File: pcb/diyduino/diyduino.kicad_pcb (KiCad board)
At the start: 2 copper layers, 42 parts, among them J1 Conn_Coaxial_Power, U1 ATMEGA328-PU, U2 L7805, Y1 16MHz

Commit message: Reworked the ditduino.
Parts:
- removed A0, A1, A2, A3, A4, A5, D10, DA2, DA3, DA4, DA5, DA6, DA7, DA8, DA9, MISO1, MOSI1, RXD1, SCK1, SCL1, SDA1, TXD1: DATA, Pin_Headers:Pin_Header_Straight_1x03_Pitch2.54mm
- removed J1: Conn_Coaxial_Power, Connectors:BARREL_JACK
- LED3: footprint LEDs:LED_D3.0mm -> LEDs:LED_Rectangular_W3.0mm_H2.0mm
- moved RESET1 37.7 mm to (148.6, 72.4), turned to 180 degrees
- moved PR2 34.7 mm to (118.1, 53.3), turned to 180 degrees
- moved LED3 29.1 mm to (120.0, 59.1)
- moved C4 26.4 mm to (123.8, 72.4), turned to 90 degrees
- moved U2 25.4 mm to (118.7, 66.0)
- moved C5 20.1 mm to (123.8, 62.9), turned to 270 degrees
- moved R1 19.1 mm to (139.7, 65.4), turned to 0 degrees
- moved FT1 12.6 mm to (113.7, 69.8), turned to 180 degrees
- moved U1 8.98 mm to (111.8, 49.5)
- moved Y1 8.47 mm to (137.2, 55.9)
- moved C3 4.96 mm to (139.7, 57.8), turned to 90 degrees
- moved C2 4.26 mm to (134.6, 59.1), turned to 0 degrees
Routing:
- net /RESET: track 19.6 -> 74.9 mm, vias 0 -> 3
- net /VCC: track 158.9 -> 198.9 mm, vias 0 -> 1
- net /VIN: track 107.4 -> 125.0 mm
- net Earth: track 15.4 -> 0.00 mm
- net /D13: track 19.2 -> 7.62 mm
- net /D12: track 18.6 -> 7.62 mm
- net /D11: track 18.1 -> 7.62 mm
- net /D10: track 18.1 -> 7.62 mm
- net /D1: track 56.0 -> 65.1 mm
- net /D5: track 20.6 -> 26.5 mm
- net /A2: track 35.8 -> 40.8 mm, vias 0 -> 1
- net /A3: track 36.9 -> 41.9 mm, vias 0 -> 1
- net Net-(C2-Pad1): track 5.94 -> 10.7 mm
- net /D3: track 35.9 -> 40.1 mm
- net /D4: track 34.6 -> 38.8 mm
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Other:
- board text added: "A0"
- board text added: "A1"
- board text added: "A2"
- board text added: "A3"
- board text added: "A4"
- board text added: "A5"
- board text added: "MISO"
- board text added: "SCK"
- board text removed: "10"
- board text removed: "11"
- board text removed: "12"
- board text removed: "13"

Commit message: Reworked diyduino module.
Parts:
- added D1: D, Diodes_THT:D_T-1_P5.08mm_Horizontal, F.Cu at (116.8, 73.0)
- added D2: D, Diodes_THT:D_T-1_P5.08mm_Horizontal, F.Cu at (122.6, 59.1)
- moved PR2 29.5 mm to (146.1, 62.9)
- moved LED3 24.4 mm to (144.1, 55.2), turned to 270 degrees
- moved R1 6.35 mm to (146.1, 65.4), turned to 180 degrees
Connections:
- FT1 pad 3: /VCC -> Net-(D1-Pad2)
- U2 pad 3: /VCC -> Net-(D2-Pad2)
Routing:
- net /VCC: track 198.9 -> 161.0 mm
- net Net-(D1-Pad2): track 0.00 -> 16.2 mm
- net Net-(D2-Pad2): track 0.00 -> 4.97 mm
- net Net-(LED3-Pad2): track 3.96 -> 5.87 mm
- net /D9: track 33.9 -> 32.9 mm
- net /D7: track 22.4 -> 23.3 mm
- net /D0: track 57.4 -> 56.9 mm

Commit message: Tidied diyduino
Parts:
- moved D1 1.91 mm to (118.7, 73.0), turned to 180 degrees
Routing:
- net Net-(D1-Pad2): track 16.2 -> 11.1 mm
- net /RESET: track 74.8 -> 72.5 mm, vias 3 -> 1
- net /D0: track 56.9 -> 58.3 mm
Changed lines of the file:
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@@
     (thickness 1.6)
     (drawings 36)
-    (tracks 222)
+    (tracks 226)
     (zones 0)
     (modules 21)
@@
   )
   (setup
-    (last_trace_width 0.25)
+    (last_trace_width 0.5)
     (user_trace_width 0.5)
     (user_trace_width 0.5)
@@
     (pad_to_mask_clearance 0)
     (aux_axis_origin 0 0)
-    (visible_elements FFFFFF7F)
+    (visible_elements FFFEFF7F)
     (pcbplotparams
       (layerselection 0x00030_80000001)
@@
     (descr "CP, Radial series, Radial, pin pitch=2.50mm, , diameter=6.3mm, Electrolytic Capacitor")
     (tags "CP Radial series Radial pin pitch 2.50mm  diameter 6.3mm Electrolytic Capacitor")
-    (fp_text reference C4 (at 1.25 -4.46 90) (layer F.SilkS)
+    (fp_text reference C4 (at -1.27 -2.54 180) (layer F.SilkS)
       (effects (font (size 1 1) (thickness 0.15)))
     )
@@
     (descr "CP, Radial series, Radial, pin pitch=2.50mm, , diameter=6.3mm, Electrolytic Capacitor")
     (tags "CP Radial series Radial pin pitch 2.50mm  diameter 6.3mm Electrolytic Capacitor")
-    (fp_text reference C5 (at 1.25 -4.46 270) (layer F.SilkS)
+    (fp_text reference C5 (at -1.27 -2.54 360) (layer F.SilkS)
       (effects (font (size 1 1) (thickness 0.15)))
     )
@@
     (descr https://www.omron.com/ecb/products/pdf/en-b3f.pdf)
     (tags "tact sw push 6mm")
-    (fp_text reference RESET1 (at 3.175 3.81 180) (layer F.SilkS)
+    (fp_text reference RESET1 (at 3.175 2.54 180) (layer F.SilkS)
       (effects (font (size 1 1) (thickness 0.15)))
     )
@@
       (effects (font (size 1 1) (thickness 0.15)))
     )
-    (fp_text user %R (at 3.25 2.25 180) (layer F.Fab)
+    (fp_text user %R (at 3.175 2.54 180) (layer F.Fab)
       (effects (font (size 1 1) (thickness 0.15)))
     )
@@
   )
   (module Diodes_THT:D_T-1_P5.08mm_Horizontal (layer F.Cu)
-    (at 116.84 73.025 270)
+    (at 118.745 73.025 180)
     (descr "D, T-1 series, Axial, Horizontal, pin pitch=5.08mm, , length*diameter=3.2*2.6mm^2, , http://www.diodes.com/_files/packages/T-1.pdf")
     (tags "D T-1 series Axial Horizontal pin pitch 5.08mm  length 3.2mm diameter 2.6mm")
-    (fp_text reference D1 (at 2.54 0 270) (layer F.SilkS)
-      (effects (font (size 1 1) (thickness 0.15)))
-    )
-    (fp_text value D (at 2.54 2.36 270) (layer F.Fab)
-      (effects (font (size 1 1) (thickness 0.15)))
-    )
-    (fp_text user %R (at 2.54 0 270) (layer F.Fab)
+    (fp_text reference D1 (at 2.54 0 180) (layer F.SilkS)
+      (effects (font (size 1 1) (thickness 0.15)))
+    )
+    (fp_text value D (at 2.54 2.36 180) (layer F.Fab)
+      (effects (font (size 1 1) (thickness 0.15)))
+    )
+    (fp_text user %R (at 2.54 0 180) (layer F.Fab)
       (effects (font (size 1 1) (thickness 0.15)))
     )
@@
     (fp_line (start 6.35 1.65) (end 6.35 -1.65) (layer F.CrtYd) (width 0.05))
     (fp_line (start 6.35 -1.65) (end -1.25 -1.65) (layer F.CrtYd) (width 0.05))
-    (pad 1 thru_hole rect (at 0 0 270) (size 2 2) (drill 1) (layers *.Cu *.Mask)
+    (pad 1 thru_hole rect (at 0 0 180) (size 2 2) (drill 1) (layers *.Cu *.Mask)
       (net 21 /VCC))
-    (pad 2 thru_hole oval (at 5.08 0 270) (size 2 2) (drill 1) (layers *.Cu *.Mask)
+    (pad 2 thru_hole oval (at 5.08 0 180) (size 2 2) (drill 1) (layers *.Cu *.Mask)
       (net 28 "Net-(D1-Pad2)"))
     (model ${KISYS3DMOD}/Diodes_THT.3dshapes/D_T-1_P5.08mm_Horizontal.wrl
@@
   (segment (start 114.935 47.625) (end 111.76 47.625) (width 0.25) (layer F.Cu) (net 14))
   (segment (start 144.78 34.29) (end 144.78 34.925) (width 0.25) (layer B.Cu) (net 14) (status 30))
-  (segment (start 113.665 59.69) (end 114.935 58.42) (width 0.25) (layer B.Cu) (net 15) (status 10))
-  (segment (start 114.935 50.165) (end 114.3 49.53) (width 0.25) (layer B.Cu) (net 15) (status 20))
-  (segment (start 114.935 58.42) (end 114.935 50.165) (width 0.25) (layer B.Cu) (net 15))
+  (segment (start 113.665 59.69) (end 113.03 59.69) (width 0.25) (layer B.Cu) (net 15))
+  (segment (start 113.03 59.69) (end 111.76 58.42) (width 0.25) (layer B.Cu) (net 15))
+  (segment (start 111.76 58.42) (end 111.76 55.245) (width 0.25) (layer B.Cu) (net 15))
+  (segment (start 111.76 55.245) (end 114.3 52.705) (width 0.25) (layer B.Cu) (net 15))
+  (segment (start 114.3 52.705) (end 114.3 49.53) (width 0.25) (layer B.Cu) (net 15))
   (via (at 133.35 39.37) (size 0.6) (drill 0.4) (layers F.Cu B.Cu) (net 15))
   (via (at 118.11 39.37) (size 0.6) (drill 0.4) (layers F.Cu B.Cu) (net 15))
@@
   (segment (start 154.94 53.975) (end 145.415 44.45) (width 0.25) (layer F.Cu) (net 20) (status 10))
   (segment (start 145.415 44.45) (end 126.365 44.45) (width 0.25) (layer F.Cu) (net 20))
-  (segment (start 138.43 62.865) (end 123.825 62.865) (width 0.5) (layer B.Cu) (net 21) (status 30))
+  (segment (start 138.43 65.405) (end 137.795 65.405) (width 0.5) (layer B.Cu) (net 21) (status C00000))
+  (segment (start 137.795 65.405) (end 135.255 62.865) (width 0.5) (layer B.Cu) (net 21) (status 400000))
+  (segment (start 135.255 62.865) (end 123.825 62.865) (width 0.5) (layer B.Cu) (net 21) (status 800000))
+  (segment (start 118.745 73.025) (end 118.745 71.755) (width 0.5) (layer F.Cu) (net 21))
+  (segment (start 121.92 64.77) (end 123.825 62.865) (width 0.5) (layer F.Cu) (net 21))
+  (segment (start 121.92 68.58) (end 121.92 64.77) (width 0.5) (layer F.Cu) (net 21))
+  (segment (start 118.745 71.755) (end 121.92 68.58) (width 0.5) (layer F.Cu) (net 21))
   (segment (start 138.43 65.405) (end 138.43 62.865) (width 0.5) (layer F.Cu) (net 21) (status 30))
   (segment (start 144.78 77.47) (end 144.78 72.39) (width 0.5) (layer F.Cu) (net 21) (status 10))
@@
   (segment (start 122.555 59.055) (end 122.555 61.595) (width 0.5) (layer F.Cu) (net 21) (status 10))
   (segment (start 122.555 61.595) (end 123.825 62.865) (width 0.5) (layer F.Cu) (net 21) (status 20))
-  (segment (start 116.84 73.025) (end 121.285 68.58) (width 0.5) (layer F.Cu) (net 21) (status 10))
-  (segment (start 121.285 65.405) (end 123.825 62.865) (width 0.5) (layer F.Cu) (net 21) (status 20))
-  (segment (start 121.285 68.58) (end 121.285 65.405) (width 0.5) (layer F.Cu) (net 21))
   (segment (start 127 48.895) (end 130.175 45.72) (width 0.25) (layer F.Cu) (net 21) (status 10))
   (segment (start 130.175 45.72) (end 132.08 43.815) (width 0.25) (layer B.Cu) (net 21))
@@
   (segment (start 134.62 49.53) (end 134.62 53.34) (width 0.25) (layer F.Cu) (net 25) (status 10))
   (segment (start 134.62 53.34) (end 137.16 55.88) (width 0.25) (layer F.Cu) (net 25) (status 20))
+  (segment (start 113.665 57.15) (end 114.3 57.15) (width 0.25) (layer B.Cu) (net 26))
+  (segment (start 114.3 57.15) (end 115.57 58.42) (width 0.25) (layer B.Cu) (net 26))
+  (segment (start 138.915 75.565) (end 142.09 72.39) (width 0.25) (layer B.Cu) (net 26))
+  (segment (start 117.475 75.565) (end 138.915 75.565) (width 0.25) (layer B.Cu) (net 26))
+  (segment (start 115.57 73.66) (end 117.475 75.565) (width 0.25) (layer B.Cu) (net 26))
+  (segment (start 115.57 58.42) (end 115.57 73.66) (width 0.25) (layer B.Cu) (net 26))
   (segment (start 146.05 65.405) (end 146.05 69.85) (width 0.25) (layer F.Cu) (net 26) (status 10))
   (segment (start 146.05 69.85) (end 148.59 72.39) (width 0.25) (layer F.Cu) (net 26) (status 20))
   (segment (start 142.09 72.39) (end 141.605 72.39) (width 0.25) (layer F.Cu) (net 26) (status 30))
-  (segment (start 141.605 72.39) (end 139.065 74.93) (width 0.25) (layer F.Cu) (net 26) (status 10))
-  (segment (start 110.49 60.325) (end 113.665 57.15) (width 0.25) (layer F.Cu) (net 26) (status 20))
-  (segment (start 110.49 70.485) (end 110.49 60.325) (width 0.25) (layer F.Cu) (net 26))
-  (via (at 110.49 70.485) (size 0.6) (drill 0.4) (layers F.Cu B.Cu) (net 26))
-  (segment (start 114.935 74.93) (end 110.49 70.485) (width 0.25) (layer B.Cu) (net 26))
-  (segment (start 139.065 74.93) (end 114.935 74.93) (width 0.25) (layer B.Cu) (net 26))
-  (via (at 139.065 74.93) (size 0.6) (drill 0.4) (layers F.Cu B.Cu) (net 26))
   (segment (start 111.76 49.53) (end 111.76 55.245) (width 0.25) (layer F.Cu) (net 26) (status 10))
   (segment (start 111.76 55.245) (end 113.665 57.15) (width 0.25) (layer F.Cu) (net 26) (status 20))
@@
   (segment (start 144.145 57.785) (end 144.145 60.96) (width 0.25) (layer F.Cu) (net 27) (status 10))
   (segment (start 144.145 60.96) (end 146.05 62.865) (width 0.25) (layer F.Cu) (net 27) (status 20))
-  (segment (start 116.84 78.105) (end 116.84 76.835) (width 0.5) (layer F.Cu) (net 28) (status 10))
-  (segment (start 111.76 66.675) (end 113.665 64.77) (width 0.5) (layer F.Cu) (net 28) (status 20))
-  (segment (start 111.76 71.755) (end 111.76 66.675) (width 0.5) (layer F.Cu) (net 28))
-  (segment (start 116.84 76.835) (end 111.76 71.755) (width 0.5) (layer F.Cu) (net 28))
+  (segment (start 113.665 73.025) (end 112.395 73.025) (width 0.5) (layer F.Cu) (net 28))
+  (segment (start 111.125 67.31) (end 113.665 64.77) (width 0.5) (layer F.Cu) (net 28))
+  (segment (start 111.125 71.755) (end 111.125 67.31) (width 0.5) (layer F.Cu) (net 28))
+  (segment (start 112.395 73.025) (end 111.125 71.755) (width 0.5) (layer F.Cu) (net 28))
   (segment (start 117.475 59.055) (end 117.475 62.23) (width 0.5) (layer F.Cu) (net 29) (status 10))
   (segment (start 117.475 62.23) (end 118.745 63.5) (width 0.5) (layer F.Cu) (net 29) (status 20))

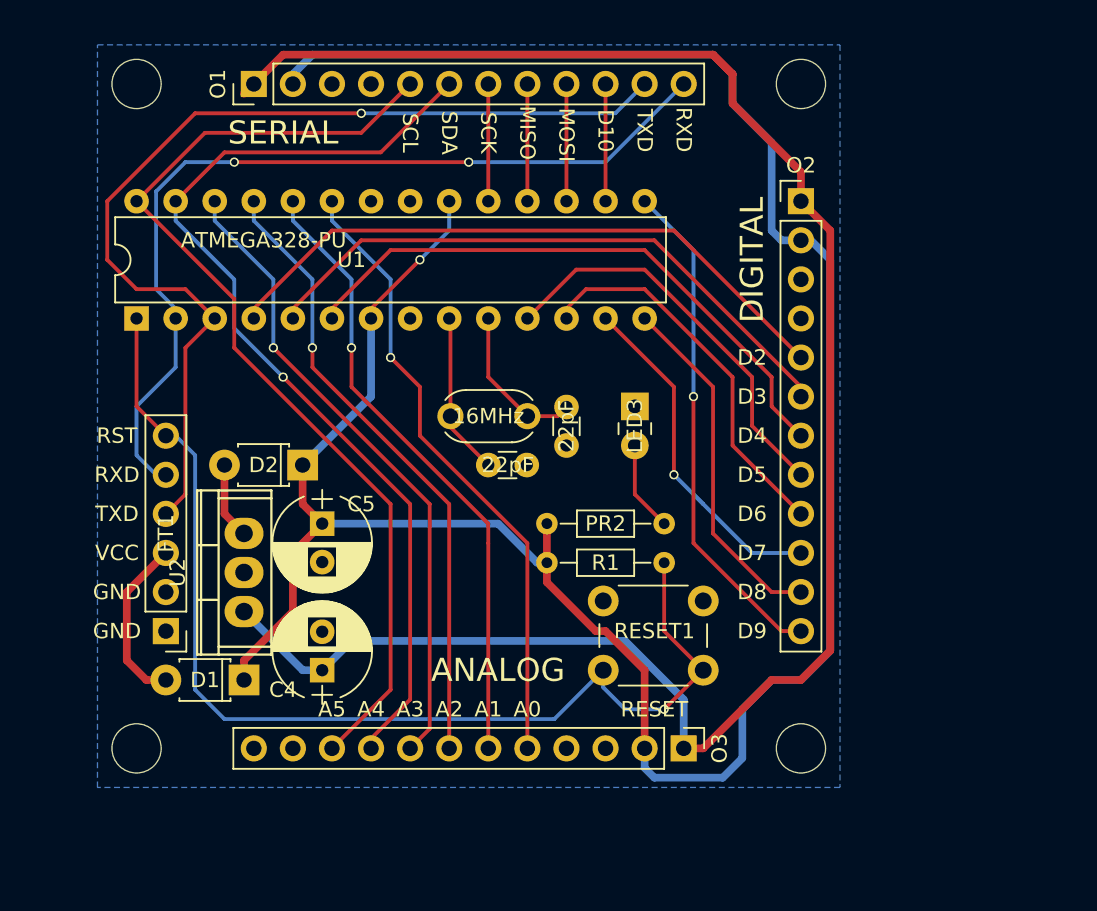
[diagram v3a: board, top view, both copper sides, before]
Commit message: Added an extra FTDI header, with the RX and TX reversed.
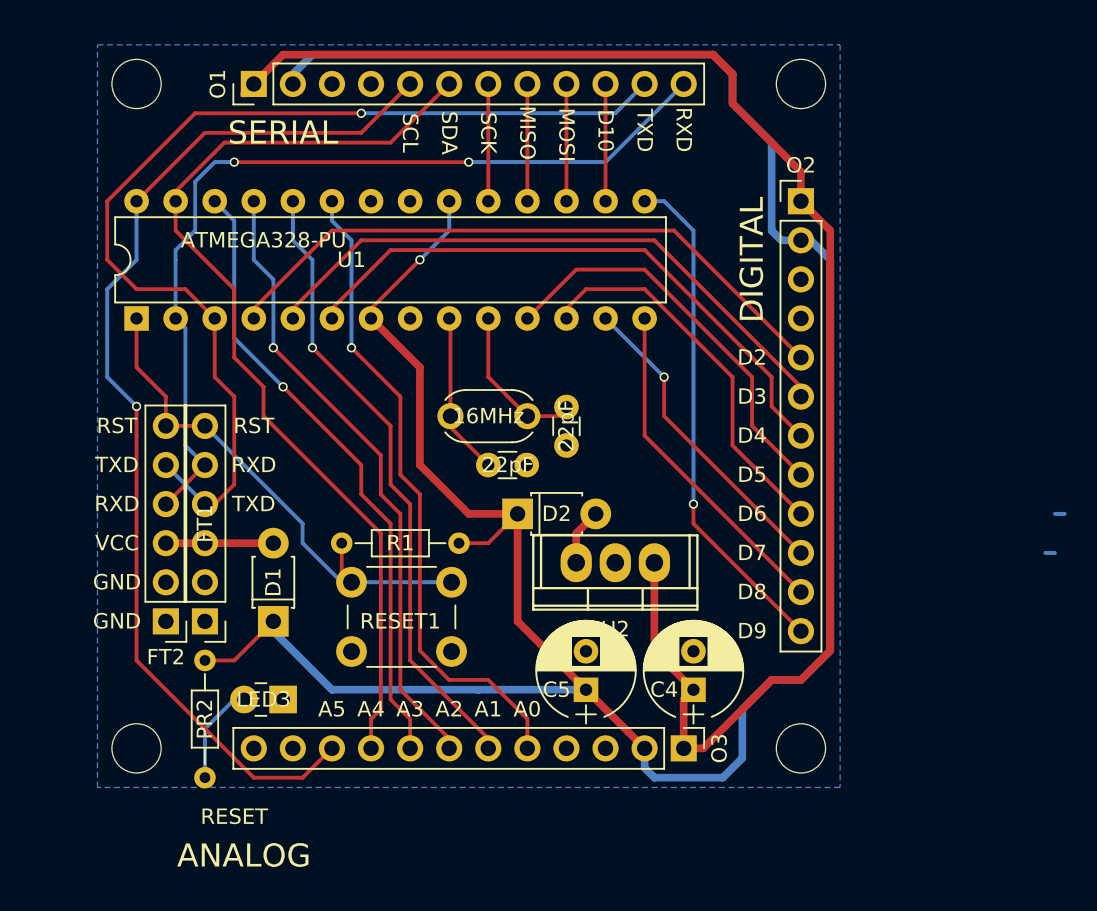
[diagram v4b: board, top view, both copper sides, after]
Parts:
- added FT2: FTDI, Pin_Headers:Pin_Header_Straight_1x06_Pitch2.54mm, F.Cu at (113.7, 69.2)
- moved PR2 34.1 mm to (116.2, 79.4), turned to 90 degrees
- moved LED3 29.8 mm to (121.3, 74.3), turned to 180 degrees
- moved C4 24.2 mm to (148.0, 73.7)
- moved U2 24.1 mm to (142.9, 65.4), turned to 180 degrees
- moved RESET1 23.6 mm to (125.7, 66.7), turned to 0 degrees
- moved R1 21.0 mm to (125.1, 64.1), turned to 0 degrees
- moved C5 20.3 mm to (141.0, 73.7), turned to 90 degrees
- moved D2 14.3 mm to (136.5, 62.2), turned to 0 degrees
- moved D1 4.26 mm to (120.7, 69.2), turned to 90 degrees
- moved FT1 2.62 mm to (116.2, 69.2)
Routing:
- net /RESET: track 72.5 -> 34.1 mm, vias 1 -> 0
- net /VIN: track 125.0 -> 102.0 mm
- net /VCC: track 161.3 -> 170.5 mm
- net Net-(D1-Pad2): track 11.1 -> 6.98 mm
- net /A5: track 65.5 -> 69.0 mm, vias 0 -> 1
- net /D1: track 65.1 -> 68.4 mm
- net /D7: track 23.3 -> 21.1 mm
- net /A0: track 40.8 -> 42.3 mm
- net Net-(D2-Pad2): track 4.97 -> 3.70 mm
- net (no net): track 0.00 -> 1.27 mm
- net /D8: track 23.1 -> 22.0 mm
- net /A3: track 41.9 -> 40.8 mm
- net /A1: track 41.5 -> 40.8 mm
- net Net-(LED3-Pad2): track 5.87 -> 6.50 mm
- net /A4: track 63.9 -> 63.3 mm, vias 1 -> 0

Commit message: Reordered serial connectors so that A4 and A5 on the analog connector are in the same place as they are on the serial connector.
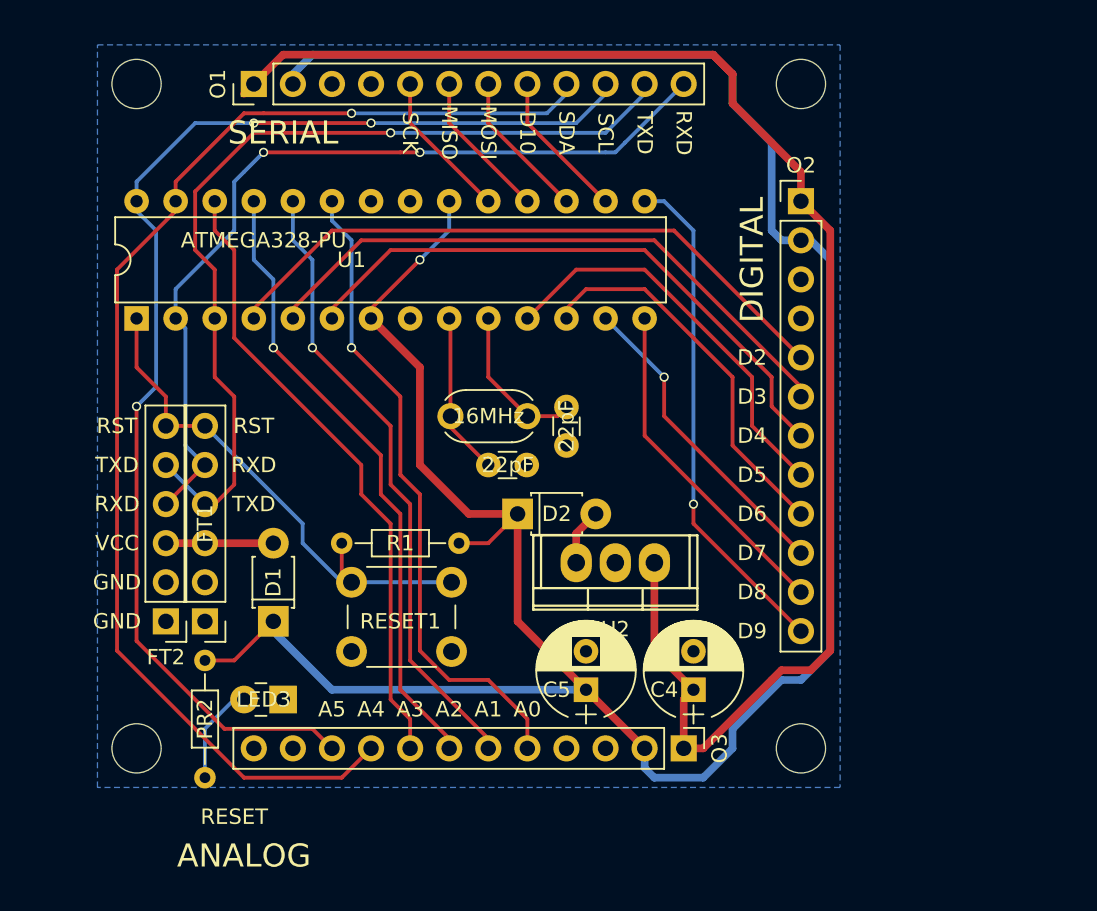
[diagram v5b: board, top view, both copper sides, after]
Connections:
- O1 pad 10: /D10 -> /A5
- O1 pad 5: /A5 -> /D13
- O1 pad 6: /A4 -> /D12
- O1 pad 7: /D13 -> /D11
- O1 pad 8: /D12 -> /D10
- O1 pad 9: /D11 -> /A4
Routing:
- net /A4: track 63.3 -> 82.4 mm, vias 0 -> 1
- net /A5: track 69.0 -> 80.0 mm, vias 1 -> 3
- net /D1: track 68.4 -> 58.6 mm
- net /D13: track 7.62 -> 9.72 mm
- net /D10: track 7.62 -> 9.72 mm
- net /D12: track 7.62 -> 9.72 mm
- net /D11: track 7.62 -> 9.72 mm
- net (no net): track 1.27 -> 0.00 mm
- net /VCC: track 170.5 -> 169.4 mm
- net /D0: track 58.3 -> 57.5 mm
- net /A3: vias 1 -> 0

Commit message: Combined multiples modules into a single board (called combined).
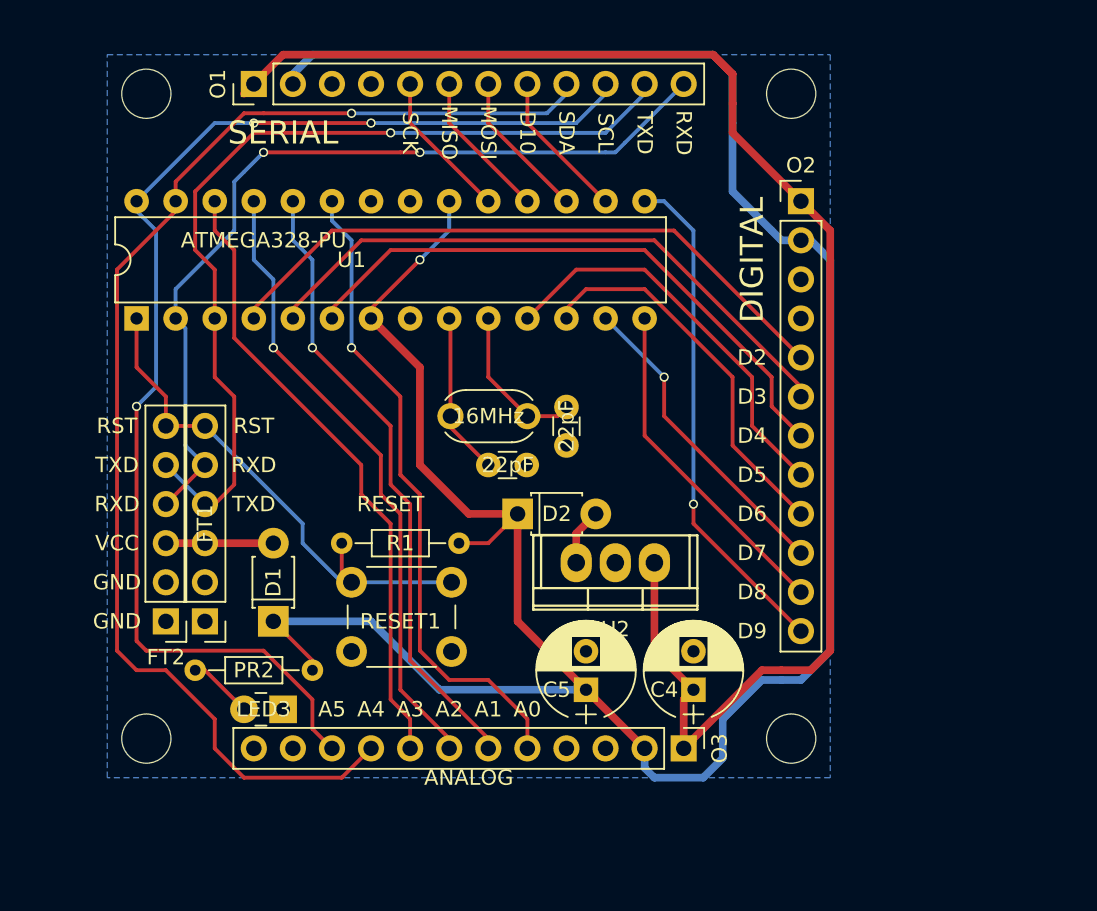
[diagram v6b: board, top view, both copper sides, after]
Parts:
- moved PR2 7.01 mm to (115.6, 72.4), turned to 0 degrees
- moved ? 0.90 mm to (154.3, 76.8)
- moved ? 0.90 mm to (112.4, 76.8)
- moved ? 0.90 mm to (154.3, 34.9)
- moved ? 0.90 mm to (112.4, 34.9)
- moved LED3 0.64 mm to (121.3, 74.9)
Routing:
- net Net-(LED3-Pad2): track 6.50 -> 4.86 mm
- net /VCC: track 169.4 -> 167.9 mm
- net /A4: track 82.4 -> 83.6 mm
